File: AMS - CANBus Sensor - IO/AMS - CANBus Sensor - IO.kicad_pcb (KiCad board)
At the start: 2 copper layers, 72.9 x 71.1 mm, 34 parts, among them J1 Power_And_CAN, J3 TTL_Programmer, J4 ICSP, J5 Conn_01x02, Q1 IRF9Z34NPBF, U1 MCP23008-xSO, U2 ATmega328P-P, U3 MCP2515-xSO, U4 MCP2551-I-SN, U5 3568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

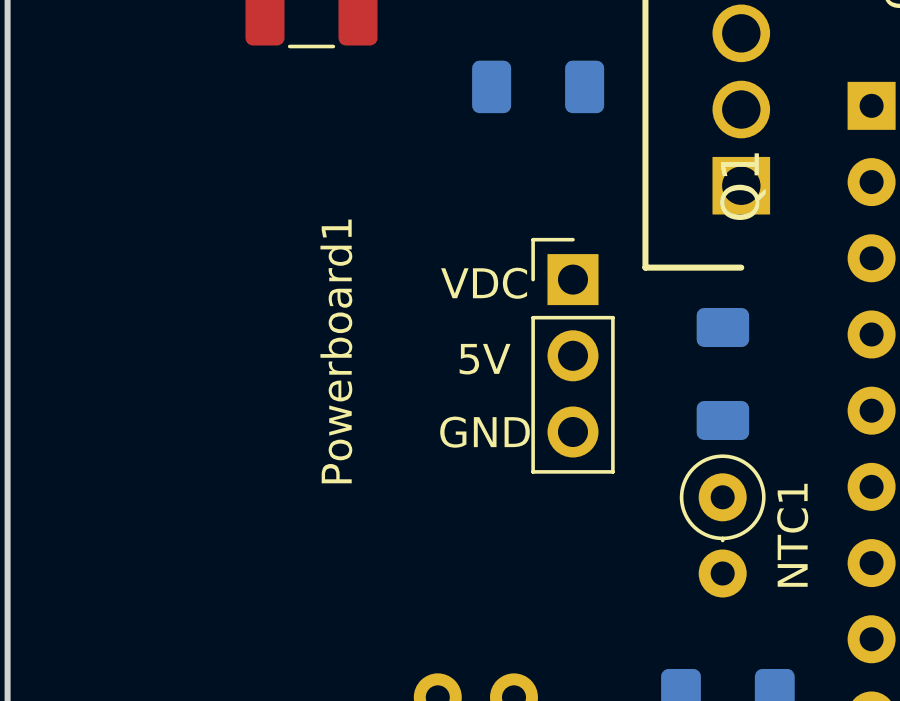
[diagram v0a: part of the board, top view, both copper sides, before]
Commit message: fixing the same powerboard problem on the remaining boards.
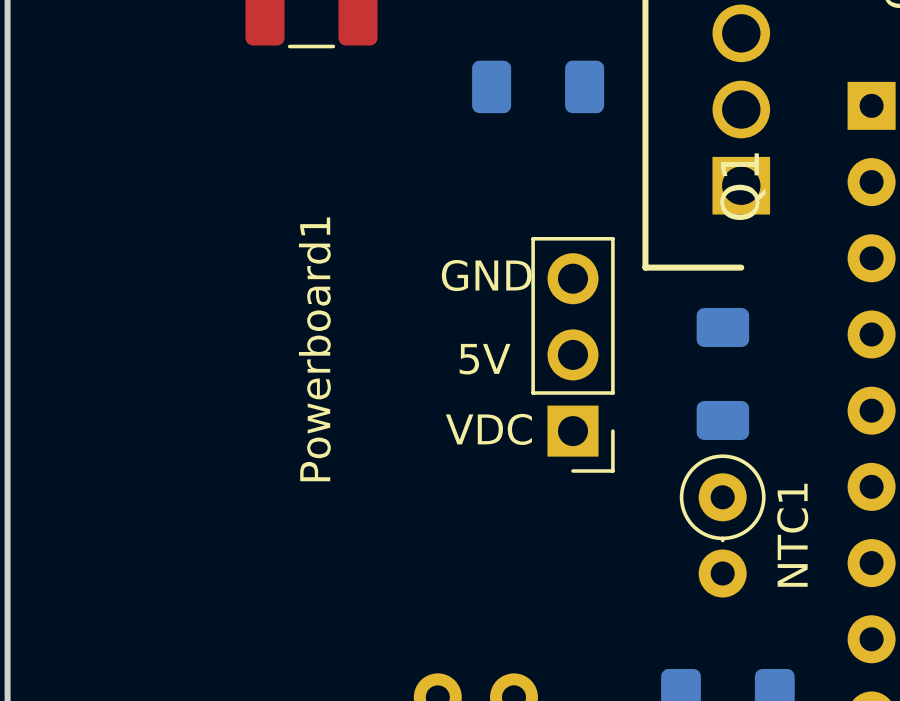
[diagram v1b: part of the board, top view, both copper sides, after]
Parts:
- moved Powerboard1 5.05 mm to (131.0, 92.6), turned to 180 degrees
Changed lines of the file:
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@@
 	(footprint "Connector_PinHeader_2.54mm:PinHeader_1x03_P2.54mm_Vertical"
 		(layer "F.Cu")
-		(at 130.9763 87.5526)
+		(at 130.9763 92.6026 180)
 		(descr "Through hole straight pin header, 1x03, 2.54mm pitch, single row")
 		(tags "Through hole pin header THT 1x03 2.54mm single row")
 		(property "Reference" "Powerboard1"
-			(at -7.839313 2.399638 90)
+			(at 8.555547 2.719984 270)
 			(layer "F.SilkS")
 			(effects
@@
 		)
 		(property "Value" "Conn_01x03"
-			(at 0 7.41 0)
+			(at 0 7.41 180)
 			(layer "F.Fab")
 			(hide yes)
@@
 		)
 		(property "Footprint" "Connector_PinHeader_2.54mm:PinHeader_1x03_P2.54mm_Vertical"
-			(at 0 0 0)
+			(at 0 0 180)
 			(unlocked yes)
 			(layer "F.Fab")
@@
 		)
 		(property "Datasheet" ""
-			(at 0 0 0)
+			(at 0 0 180)
 			(unlocked yes)
 			(layer "F.Fab")
@@
 		)
 		(property "Description" "Generic connector, single row, 01x03, script generated (kicad-library-utils/schlib/autogen/connector/)"
-			(at 0 0 0)
+			(at 0 0 180)
 			(unlocked yes)
 			(layer "F.Fab")
@@
 		(attr through_hole)
 		(fp_line
-			(start -1.33 -1.33)
-			(end 0 -1.33)
+			(start 1.33 1.27)
+			(end 1.33 6.41)
 			(stroke
 				(width 0.12)
@@
 		)
 		(fp_line
-			(start -1.33 0)
-			(end -1.33 -1.33)
+			(start -1.33 6.41)
+			(end 1.33 6.41)
 			(stroke
 				(width 0.12)
@@
 		(fp_line
 			(start -1.33 1.27)
-			(end -1.33 6.41)
+			(end 1.33 1.27)
 			(stroke
 				(width 0.12)
@@
 		(fp_line
 			(start -1.33 1.27)
-			(end 1.33 1.27)
+			(end -1.33 6.41)
 			(stroke
 				(width 0.12)
@@
 		)
 		(fp_line
-			(start -1.33 6.41)
-			(end 1.33 6.41)
+			(start -1.33 0)
+			(end -1.33 -1.33)
 			(stroke
 				(width 0.12)
@@
 		)
 		(fp_line
-			(start 1.33 1.27)
-			(end 1.33 6.41)
+			(start -1.33 -1.33)
+			(end 0 -1.33)
 			(stroke
 				(width 0.12)
@@
 		)
 		(fp_line
-			(start -1.8 -1.8)
-			(end -1.8 6.85)
+			(start 1.8 6.85)
+			(end 1.8 -1.8)
 			(stroke
 				(width 0.05)
@@
 		)
 		(fp_line
-			(start -1.8 6.85)
-			(end 1.8 6.85)
+			(start 1.8 -1.8)
+			(end -1.8 -1.8)
 			(stroke
 				(width 0.05)
@@
 		)
 		(fp_line
-			(start 1.8 -1.8)
-			(end -1.8 -1.8)
+			(start -1.8 6.85)
+			(end 1.8 6.85)
 			(stroke
 				(width 0.05)
@@
 		)
 		(fp_line
-			(start 1.8 6.85)
-			(end 1.8 -1.8)
+			(start -1.8 -1.8)
+			(end -1.8 6.85)
 			(stroke
 				(width 0.05)
@@
 		)
 		(fp_line
-			(start -1.27 -0.635)
-			(end -0.635 -1.27)
+			(start 1.27 6.35)
+			(end -1.27 6.35)
 			(stroke
 				(width 0.1)
@@
 		)
 		(fp_line
-			(start -1.27 6.35)
-			(end -1.27 -0.635)
+			(start 1.27 -1.27)
+			(end 1.27 6.35)
 			(stroke
 				(width 0.1)
@@
 		)
 		(fp_line
-			(start 1.27 -1.27)
-			(end 1.27 6.35)
+			(start -1.27 6.35)
+			(end -1.27 -0.635)
 			(stroke
 				(width 0.1)
@@
 		)
 		(fp_line
-			(start 1.27 6.35)
-			(end -1.27 6.35)
+			(start -1.27 -0.635)
+			(end -0.635 -1.27)
 			(stroke
 				(width 0.1)
@@
 		)
 		(fp_text user "${REFERENCE}"
-			(at -2.635793 2.19541 90)
+			(at -2.635793 2.19541 270)
 			(layer "F.Fab")
 			(effects
@@
 		)
 		(pad "1" thru_hole rect
-			(at 0 0)
+			(at 0 0 180)
 			(size 1.7 1.7)
 			(drill 1)
@@
 		)
 		(pad "2" thru_hole oval
-			(at 0 2.54)
+			(at 0 2.54 180)
 			(size 1.7 1.7)
 			(drill 1)
@@
 		)
 		(pad "3" thru_hole oval
-			(at 0 5.08)
+			(at 0 5.08 180)
 			(size 1.7 1.7)
 			(drill 1)
@@
 	)
 	(gr_text "GND"
-		(at 126.47268 93.259882 0)
+		(at 126.527843 88.038616 0)
 		(layer "F.SilkS")
 		(effects
@@
 	)
 	(gr_text "VDC"
-		(at 126.567918 88.296655 0)
+		(at 126.729007 93.168288 0)
 		(layer "F.SilkS")
 		(effects
